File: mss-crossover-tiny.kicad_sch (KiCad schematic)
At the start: 31 parts, among them J1 RJ45, J2 RJ45, J3 Screw_Terminal_01x02, J4 Screw_Terminal_01x02, J5 Screw_Terminal_01x02, J6 ISP (3V3), J7 Screw_Terminal_01x02, SW1 Set, U1 TLP187, U2 AMS1117-3.3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

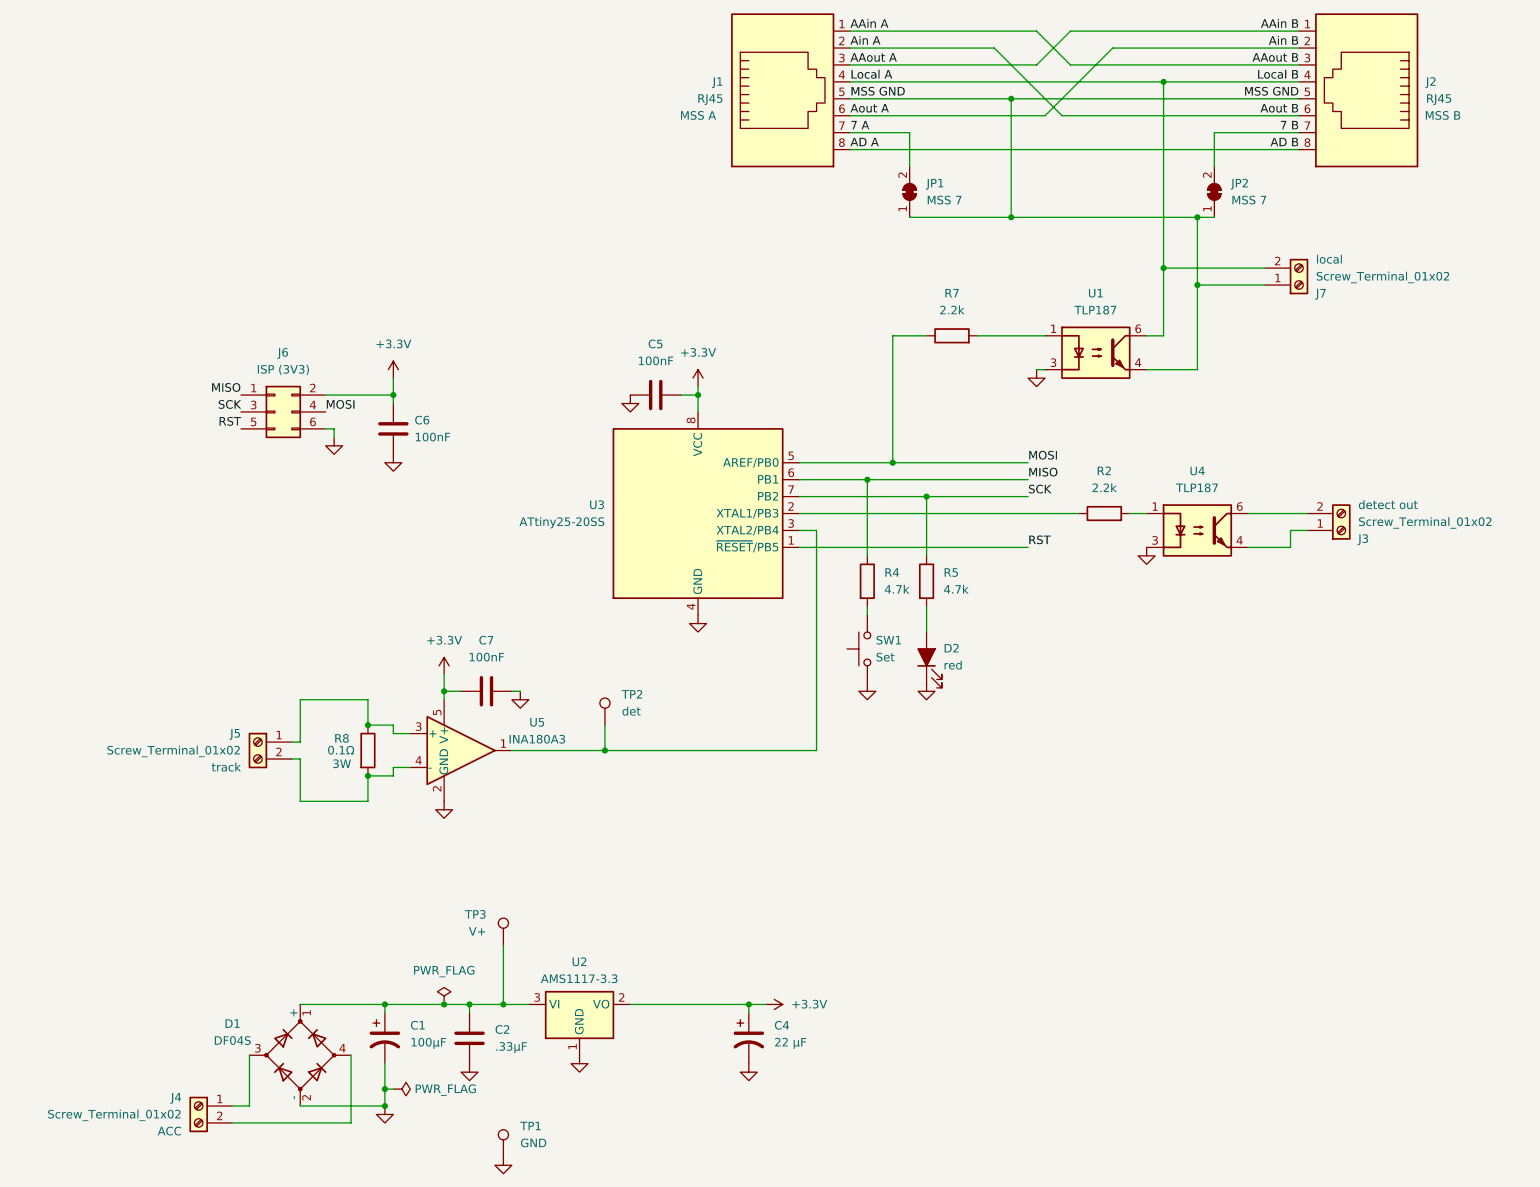
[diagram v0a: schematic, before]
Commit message: Updated to KiCad v9.  This is the release that was sent to JLCPCB for assembly as version 4.0.
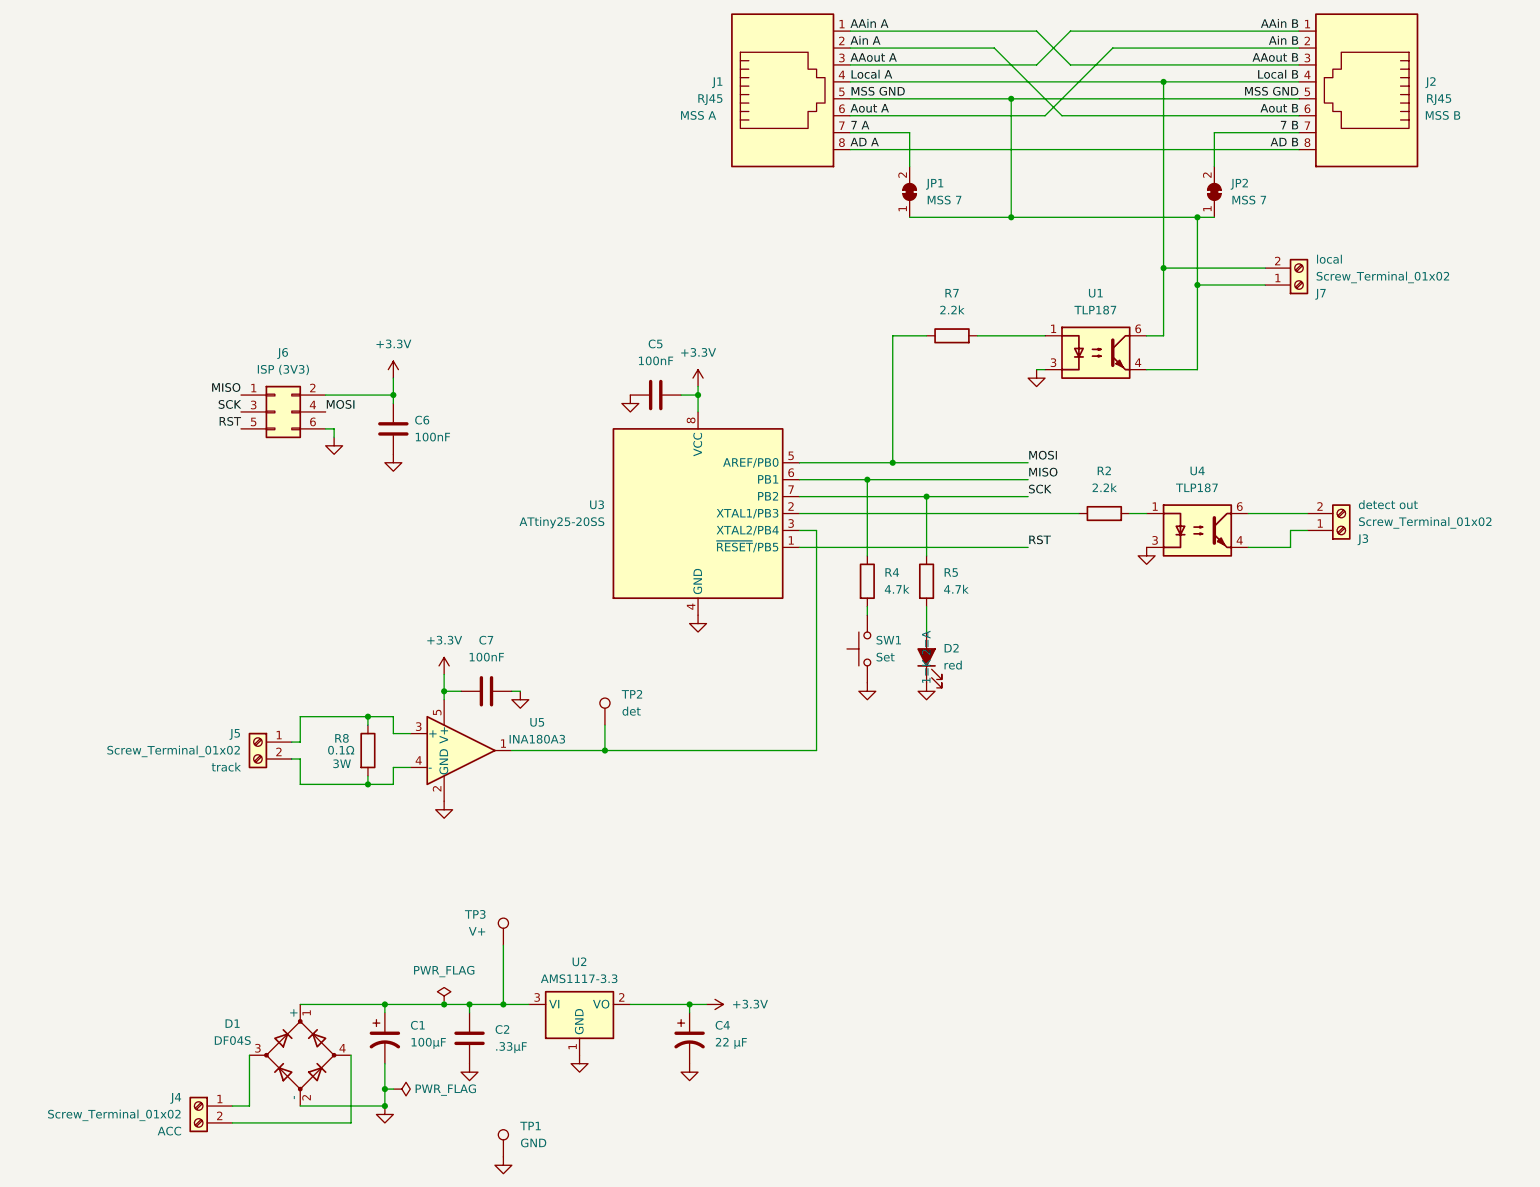
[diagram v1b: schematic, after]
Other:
- moved on the sheet: C4
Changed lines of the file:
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@@
 (kicad_sch
-	(version 20231120)
+	(version 20250114)
 	(generator "eeschema")
-	(generator_version "8.0")
+	(generator_version "9.0")
 	(paper "A")
 	(title_block
 		(title "MSS Crossover Node")
 		(date "2024-03-23")
-		(rev "3.0")
-	)
-	(junction
-		(at 73.66 140.97)
-		(diameter 0)
-		(color 0 0 0 0)
+		(rev "4.0")
 	)
 	(junction
@@
 	)
 	(junction
-		(at 76.2 175.26)
+		(at 73.66 132.08)
 		(diameter 0)
 		(color 0 0 0 0)
 	)
 	(junction
-		(at 148.59 96.52)
+		(at 76.2 175.26)
 		(diameter 0)
 		(color 0 0 0 0)
 	)
 	(junction
-		(at 73.66 133.35)
+		(at 148.59 96.52)
 		(diameter 0)
 		(color 0 0 0 0)
@@
 	)
 	(junction
-		(at 130.81 175.26)
+		(at 121.92 175.26)
+		(diameter 0)
+		(color 0 0 0 0)
+	)
+	(junction
+		(at 73.66 142.24)
 		(diameter 0)
 		(color 0 0 0 0)
@@
 	(wire
 		(pts
-			(xy 63.5 144.78) (xy 63.5 138.43)
+			(xy 63.5 142.24) (xy 63.5 138.43)
 		)
 		(stroke
@@
 	(wire
 		(pts
-			(xy 73.66 140.97) (xy 77.47 140.97)
+			(xy 73.66 142.24) (xy 77.47 142.24)
 		)
 		(stroke
@@
 	(wire
 		(pts
-			(xy 88.9 175.26) (xy 93.98 175.26)
+			(xy 73.66 132.08) (xy 73.66 133.35)
 		)
 		(stroke
@@
 	(wire
 		(pts
-			(xy 73.66 133.35) (xy 77.47 133.35)
+			(xy 88.9 175.26) (xy 93.98 175.26)
 		)
 		(stroke
@@
 	(wire
 		(pts
-			(xy 77.47 139.7) (xy 80.01 139.7)
+			(xy 73.66 132.08) (xy 77.47 132.08)
 		)
 		(stroke
@@
 	(wire
 		(pts
-			(xy 146.05 31.75) (xy 167.64 31.75)
+			(xy 77.47 139.7) (xy 80.01 139.7)
 		)
 		(stroke
@@
 	(wire
 		(pts
-			(xy 198.12 80.01) (xy 198.12 67.31)
+			(xy 146.05 31.75) (xy 167.64 31.75)
 		)
 		(stroke
@@
 	(wire
 		(pts
-			(xy 73.66 144.78) (xy 73.66 140.97)
+			(xy 198.12 80.01) (xy 198.12 67.31)
 		)
 		(stroke
@@
 	(wire
 		(pts
-			(xy 77.47 133.35) (xy 77.47 134.62)
+			(xy 77.47 132.08) (xy 77.47 134.62)
 		)
 		(stroke
@@
 	(wire
 		(pts
-			(xy 73.66 129.54) (xy 73.66 133.35)
-		)
-		(stroke
-			(width 0)
-			(type default)
-		)
-	)
-	(wire
-		(pts
 			(xy 157.48 99.06) (xy 157.48 107.95)
 		)
@@
 	(wire
 		(pts
-			(xy 77.47 140.97) (xy 77.47 139.7)
+			(xy 77.47 142.24) (xy 77.47 139.7)
 		)
 		(stroke
@@
 	(wire
 		(pts
-			(xy 113.03 175.26) (xy 130.81 175.26)
+			(xy 113.03 175.26) (xy 121.92 175.26)
 		)
 		(stroke
@@
 	(wire
 		(pts
-			(xy 130.81 175.26) (xy 133.35 175.26)
+			(xy 121.92 175.26) (xy 124.46 175.26)
 		)
 		(stroke
@@
 	(wire
 		(pts
-			(xy 130.81 175.26) (xy 130.81 176.53)
+			(xy 121.92 175.26) (xy 121.92 176.53)
 		)
 		(stroke
@@
 	(wire
 		(pts
-			(xy 63.5 135.89) (xy 63.5 129.54)
+			(xy 63.5 135.89) (xy 63.5 132.08)
 		)
 		(stroke
@@
 	(wire
 		(pts
-			(xy 63.5 144.78) (xy 73.66 144.78)
+			(xy 63.5 142.24) (xy 73.66 142.24)
+		)
+		(stroke
+			(width 0)
+			(type default)
+		)
+	)
+	(wire
+		(pts
+			(xy 73.66 142.24) (xy 73.66 140.97)
 		)
 		(stroke
@@
 	(wire
 		(pts
-			(xy 63.5 129.54) (xy 73.66 129.54)
+			(xy 63.5 132.08) (xy 73.66 132.08)
 		)
 		(stroke
@@
 			)
 		)
-		(property "Description" ""
+		(property "Description" "Power symbol creates a global label with name \"GND\" , ground"
 			(at 96.52 128.27 0)
 			(effects
@@
 			)
 		)
-		(property "Description" ""
+		(property "Description" "Power symbol creates a global label with name \"GND\" , ground"
 			(at 123.19 116.84 0)
 			(effects
@@
 			)
 		)
-		(property "Description" ""
+		(property "Description" "Light emitting diode, filled shape"
 			(at 157.48 123.19 0)
 			(effects
@@
 			)
 		)
+		(property "Sim.Pins" "1=K 2=A"
+			(at 157.48 123.19 0)
+			(effects
+				(font
+					(size 1.27 1.27)
+				)
+			)
+		)
 		(pin "1"
 		)
@@
 			)
 		)
-		(property "Description" ""
+		(property "Description" "Power symbol creates a global label with name \"GND\" , ground"
 			(at 105.41 182.88 0)
 			(effects
@@
 			)
 		)
-		(property "Description" ""
+		(property "Description" "Power symbol creates a global label with name \"GND\" , ground"
 			(at 148.59 127 0)
 			(effects
@@
 			)
 		)
-		(property "Description" ""
+		(property "Description" "Power symbol creates a global label with name \"GND\" , ground"
 			(at 93.98 198.12 0)
 			(effects
@@
 			)
 		)
-		(property "Description" ""
+		(property "Description" "Power symbol creates a global label with name \"GND\" , ground"
 			(at 113.03 83.82 0)
 			(effects
@@
 			)
 		)
-		(property "Description" ""
+		(property "Description" "Power symbol creates a global label with name \"GND\" , ground"
 			(at 76.2 190.5 0)
 			(effects
@@
 			)
 		)
-		(property "Description" ""
+		(property "Description" "Power symbol creates a global label with name \"GND\" , ground"
 			(at 190.5 106.68 0)
 			(effects
@@
 			)
 		)
-		(property "Description" ""
+		(property "Description" "Power symbol creates a global label with name \"GND\" , ground"
 			(at 88.9 184.15 0)
 			(effects
@@
 			)
 		)
-		(property "Description" ""
+		(property "Description" "Power symbol creates a global label with name \"GND\" , ground"
 			(at 173.99 80.01 0)
 			(effects
@@
 	(symbol
 		(lib_id "power:GND")
-		(at 130.81 184.15 0)
+		(at 121.92 184.15 0)
 		(unit 1)
 		(exclude_from_sim no)
@@
 		(fields_autoplaced yes)
 		(property "Reference" "#PWR05"
-			(at 130.81 190.5 0)
+			(at 121.92 190.5 0)
 			(effects
 				(font
@@
 		)
 		(property "Value" "GND"
-			(at 130.81 189.23 0)
+			(at 121.92 189.23 0)
 			(effects
 				(font
@@
 		)
 		(property "Footprint" ""
-			(at 130.81 184.15 0)
+			(at 121.92 184.15 0)
 			(effects
 				(font
@@
 		)
 		(property "Datasheet" ""
-			(at 130.81 184.15 0)
+			(at 121.92 184.15 0)
 			(effects
 				(font
@@
 			)
 		)
-		(property "Description" ""
-			(at 130.81 184.15 0)
+		(property "Description" "Power symbol creates a global label with name \"GND\" , ground"
+			(at 121.92 184.15 0)
 			(effects
 				(font
@@
 	(symbol
 		(lib_id "power:+3.3V")
-		(at 133.35 175.26 270)
+		(at 124.46 175.26 270)
 		(unit 1)
 		(exclude_from_sim no)
@@
 		(fields_autoplaced yes)
 		(property "Reference" "#PWR017"
-			(at 129.54 175.26 0)
+			(at 120.65 175.26 0)
 			(effects
 				(font
@@
 		)
 		(property "Value" "+3.3V"
-			(at 137.16 175.2599 90)
+			(at 128.27 175.2599 90)
 			(effects
 				(font
@@
 		)
 		(property "Footprint" ""
-			(at 133.35 175.26 0)
+			(at 124.46 175.26 0)
 			(effects
 				(font
@@
 		)
 		(property "Datasheet" ""
-			(at 133.35 175.26 0)
+			(at 124.46 175.26 0)
 			(effects
 				(font
@@
 		)
 		(property "Description" "Power symbol creates a global label with name \"+3.3V\""
-			(at 133.35 175.26 0)
+			(at 124.46 175.26 0)
 			(effects
 				(font
@@
 			)
 		)
-		(property "Description" ""
+		(property "Description" "Power symbol creates a global label with name \"GND\" , ground"
 			(at 68.58 90.17 0)
 			(effects
@@
 			)
 		)
-		(property "Description" ""
+		(property "Description" "Power symbol creates a global label with name \"GND\" , ground"
 			(at 157.48 127 0)
 			(effects
@@
 			)
 		)
-		(property "Description" ""
+		(property "Description" "Power symbol creates a global label with name \"GND\" , ground"
 			(at 77.47 92.71 0)
 			(effects
@@
 	(symbol
 		(lib_id "Device:C_Polarized_US")
-		(at 130.81 180.34 0)
+		(at 121.92 180.34 0)
 		(unit 1)
 		(exclude_from_sim no)
@@
 		(fields_autoplaced yes)
 		(property "Reference" "C4"
-			(at 134.62 178.4349 0)
+			(at 125.73 178.4349 0)
 			(effects
 				(font
@@
 		)
 		(property "Value" "22 µF"
-			(at 134.62 180.9749 0)
+			(at 125.73 180.9749 0)
 			(effects
 				(font
@@
 		)
 		(property "Footprint" "Capacitor_Tantalum_SMD:CP_EIA-3216-18_Kemet-A_Pad1.58x1.35mm_HandSolder"
-			(at 130.81 180.34 0)
+			(at 121.92 180.34 0)
 			(effects
 				(font
@@
 		)
 		(property "Datasheet" "~"
-			(at 130.81 180.34 0)
+			(at 121.92 180.34 0)
 			(effects
 				(font
@@
 		)
 		(property "Description" ""
-			(at 130.81 180.34 0)
+			(at 121.92 180.34 0)
 			(effects
 				(font
@@
 		)
 		(property "MPN" ""
-			(at 130.81 180.34 0)
+			(at 121.92 180.34 0)
 			(effects
 				(font
@@
 		)
 		(property "JLCPCB Part" "C7183"
-			(at 130.81 180.34 0)
+			(at 121.92 180.34 0)
 			(effects
 				(font
@@
 		)
 		(property "FT Rotation Offset" "180"
-			(at 130.81 180.34 0)
+			(at 121.92 180.34 0)
 			(effects
 				(font
@@
 		)
 		(property "FT Position Offset" ""
-			(at 130.81 180.34 0)
+			(at 121.92 180.34 0)
 			(effects
 				(font
@@
 			)
 		)
-		(property "Description" ""
+		(property "Description" "Power symbol creates a global label with name \"GND\" , ground"
 			(at 85.09 144.78 0)
 			(effects
@@
 		)
 	)
+	(embedded_fonts no)
 )

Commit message: Some small changes learned from the first prototype.  Switch back to the larger screw terminals and changed resistor to the pushbutton to 2.2k instead of 4.7k.
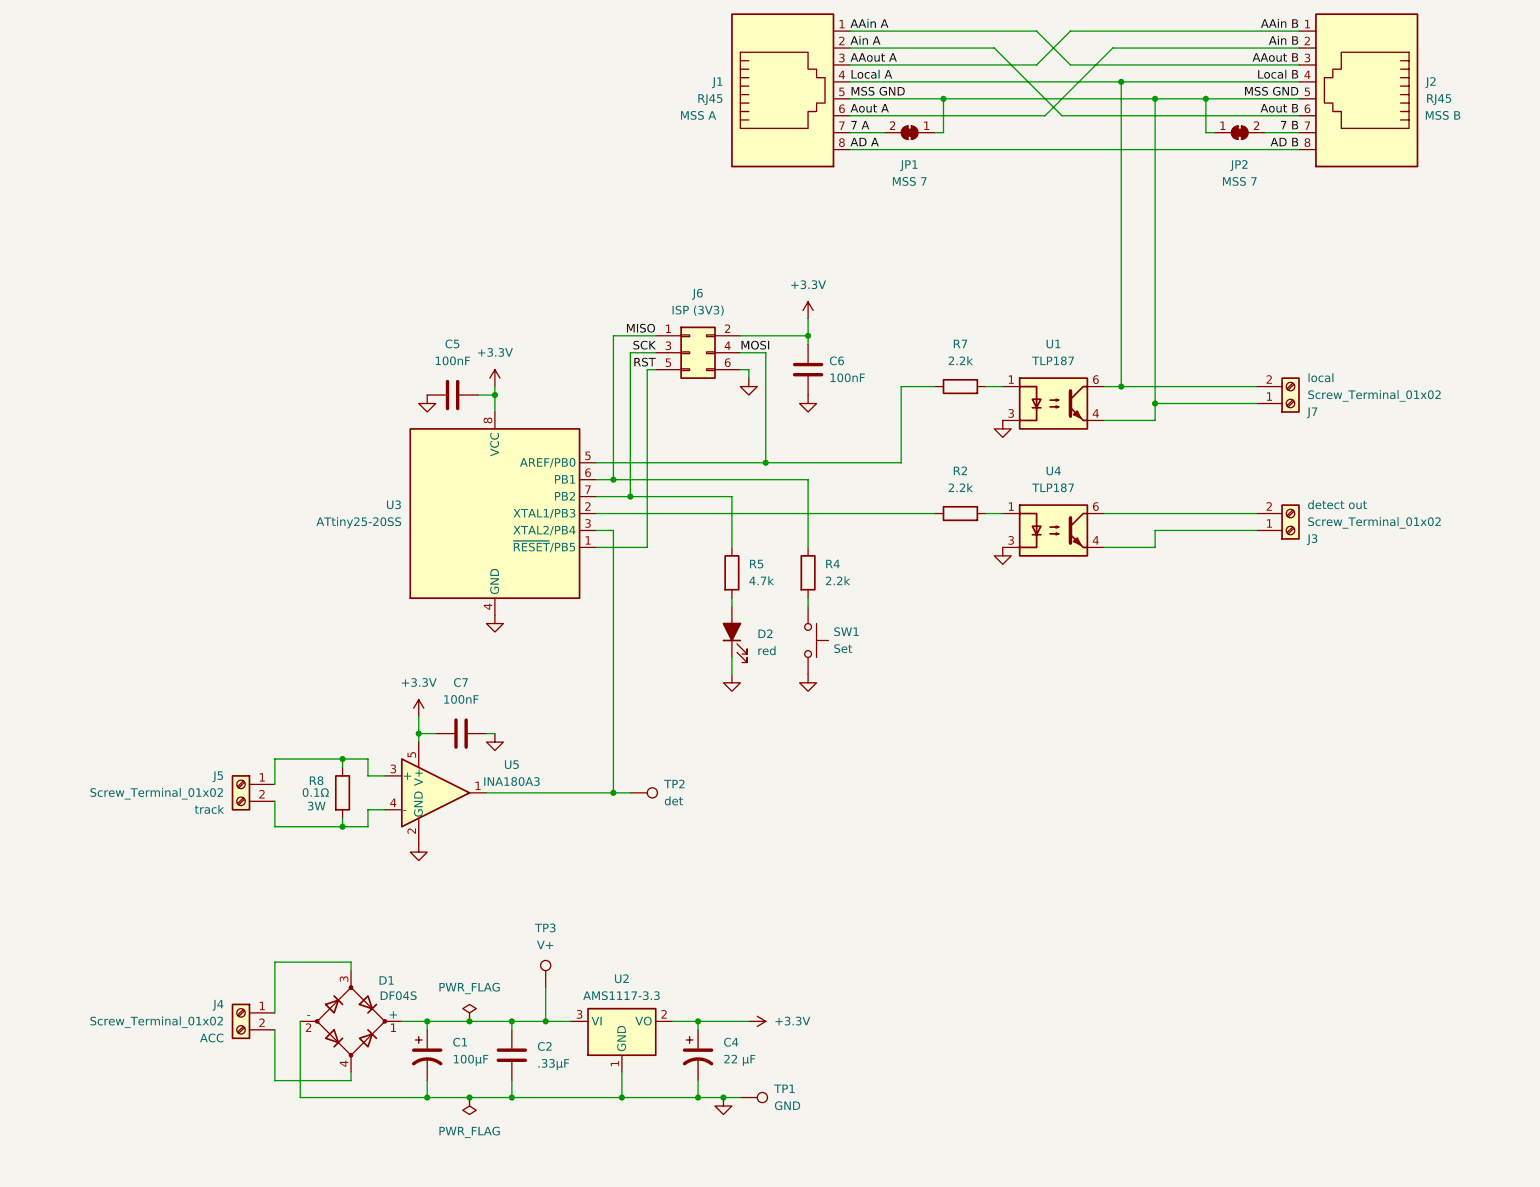
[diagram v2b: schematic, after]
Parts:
- J3, J4, J5, J7: footprint Imports:691210910002 -> Imports:CUI_TB003-500-P02BE
- R2, R7: MPN RC0805FR-101KL -> RC0805FR-102K2L
- R4: value 4.7k -> 2.2k; MPN RC0805FR-104K7L -> RC0805FR-102K2L
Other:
- moved on the sheet: C1, C2, C4, C5, C6, C7, D1, D2, J3, J4, J5, J6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
